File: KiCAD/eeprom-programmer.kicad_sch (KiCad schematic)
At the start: 8 parts

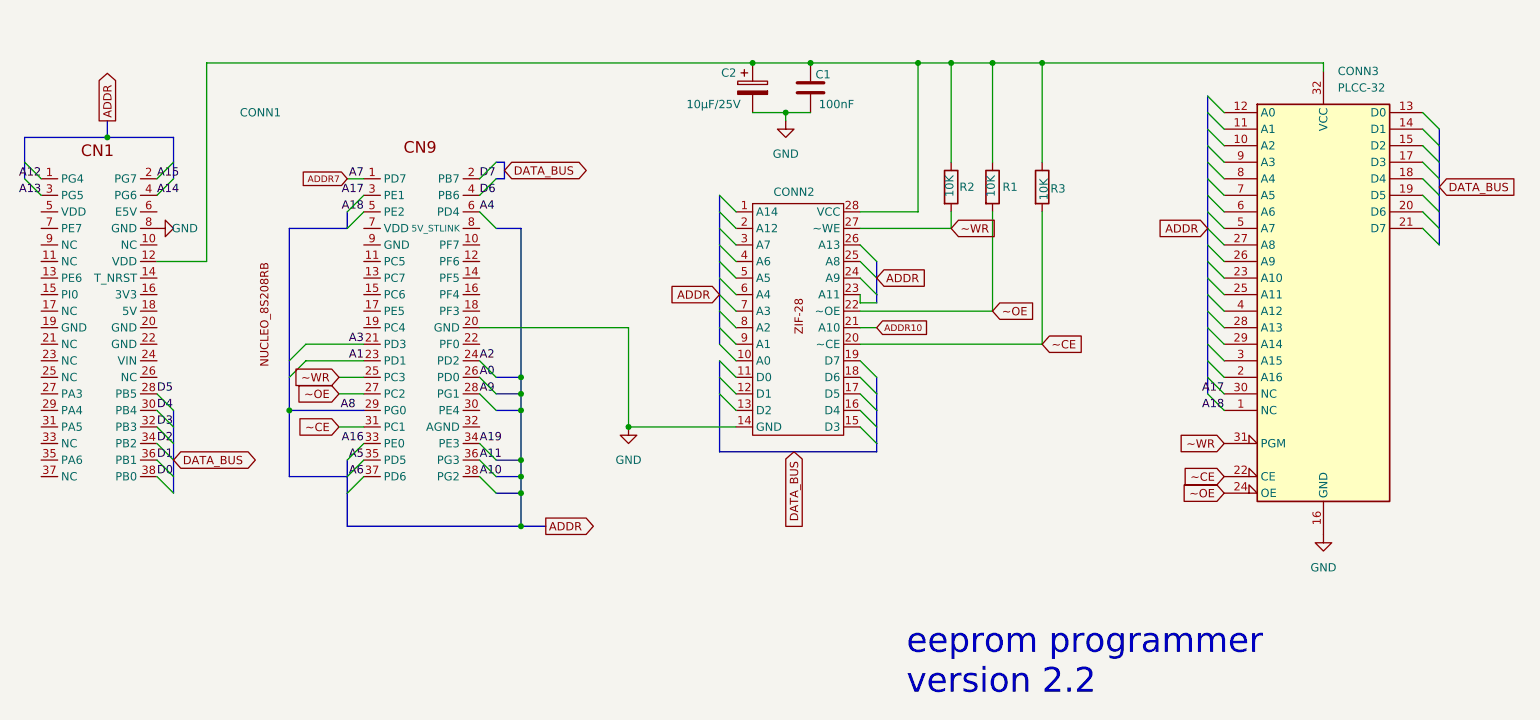
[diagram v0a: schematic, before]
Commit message: Circuit version 2.3 > Modification du circuit pour ajouter un contrôle sur l'alimentation de l'EEPROM ce qui > permet d'installer et d'enlever l'EEPROM du programmeur sans avoir à le débrancher modification du firmware pour ajouter la commande V pour contrôler le Vcc de l'EEPROM
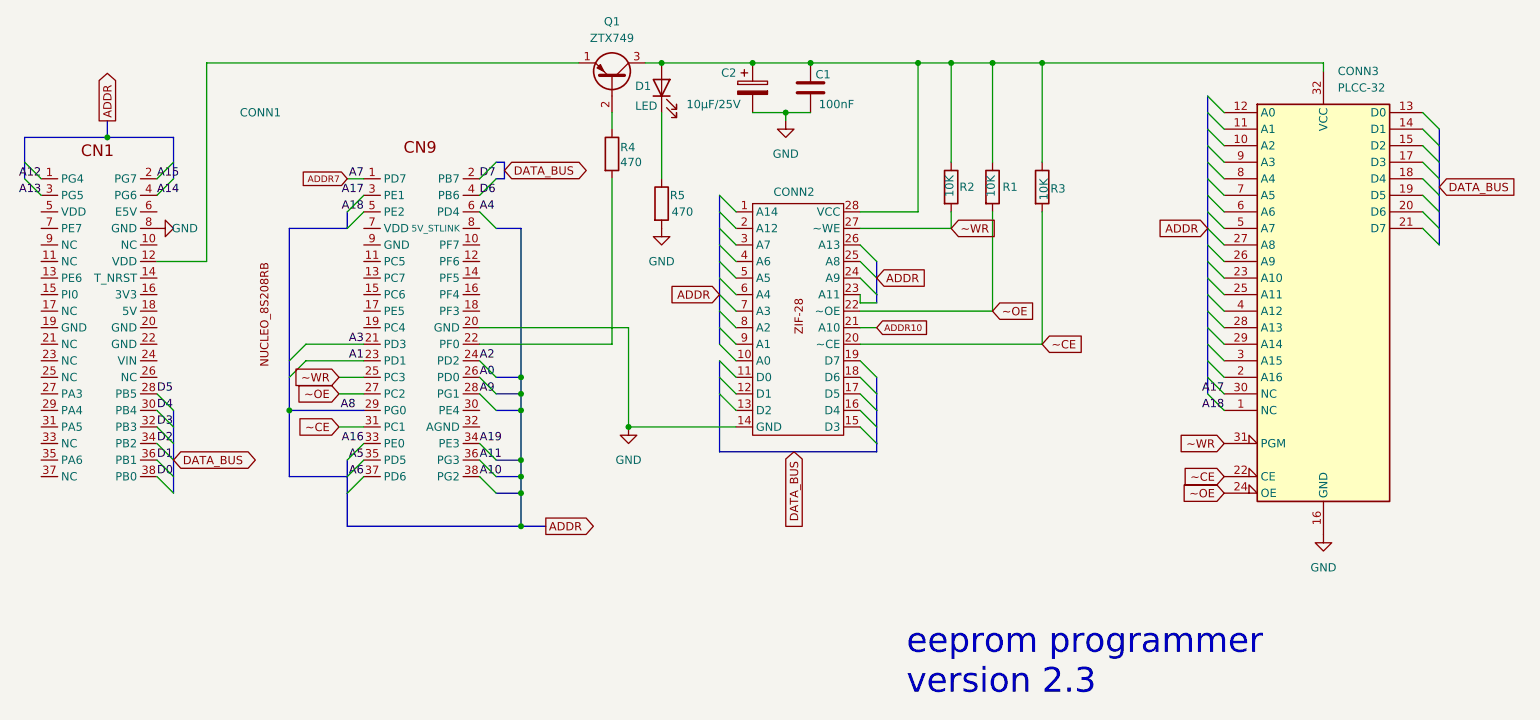
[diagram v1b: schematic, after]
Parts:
- added D1: LED, symbol Device:LED
- added Q1: ZTX749, Package_TO_SOT_THT:TO-92_Inline, symbol Transistor_BJT:2N3906
- added R4, R5: 470, symbol Device:R
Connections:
- net GND: now also R5.2
- net at C1.1, C2.1, CONN2.28 (VCC)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: now also D1.2 (A), Q1.3 (C); no longer CONN1.12 (VDD)
- net at CONN1.12 (PF6): now also Q1.1 (E)
- new net: D1.1 (K), R5.1
- new net: Q1.2 (B), R4.1
- new net: CONN1.22 (PF0), R4.2
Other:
- note added: "eeprom programmer version 2.3"
- note removed: "eeprom programmer version 2.2"
